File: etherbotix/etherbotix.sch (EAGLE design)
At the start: 28 parts, among them J1 J3011G21DNL, J2 22-03-5035, J3 22-03-5035, J4 22-03-5045, J5 22-03-5045, J6 1760520000, J7 1760490000, J8 502443-0470, J9 502443-0470, U1 STM32F407V, U2 TLK110, U3 OKI-78SR-5/1.5-W36-C, U4 TLV1117-33IKVURG3KVU, U5 ACS711ELCTR-25AB-T, U6 ACS711ELCTR-25AB-T, U7 MAX481CSA, U8 74LS126D, X1 25MHZ

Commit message: routed, still needs cleanup
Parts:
- added ACT: BLUE, fergs:APT1608SGC
- added C1, C2: 2.2uF, fergs:C1608X5R1C225K
- added C10, C14, C15, C16, C23, C24, C25, C26, C3, C36, C37, C38, C5, C6, C7, C8, C9: 0.1uF, fergs:C1608X7R1H104K
- added C11, C27, C28, C31: 4.7uF, fergs:C1608X5R0J475K
- added C12, C19, C20, C21, C22: 1uF, fergs:C1608X5R1H105M
- added C13, C17, C18, C39, C4, C40: 100pF, fergs:C1608C0G1H101J
- added C29, C30, C32: 1000PF, fergs:C1608X7R1H102K
- added C33, C34, C35: 10uF, fergs:C1608X5R0J106M
- added C41: 56uF, fergs:25SVPF56M
- added ERR: RED, fergs:APT1608SGC
- added PWR: GREEN, fergs:APT1608SGC
- added R10, R11, R12, R13, R5, R6, R7, R9: 10k, fergs:P10.0KHCT-ND
- added R14, R15, R16, R17: 49R9, fergs:P49.9HCT-ND
- added R18, R21, R23, R29: 2K2, fergs:P2.20KHCT-ND
- added R19, R20, R24, R25, R26, R28, R8: 1k, fergs:P1.00KHCT-ND
- added R22: 4K87, fergs:P4.87KHCT-ND
- added R27: 15k, fergs:P15.0KHCT-ND
- added R30: 120, fergs:P120HCT-ND
- added R31, R32: 750, fergs:P750HCT-ND
- added X2: (no value), ethernet:ASEMB-50.000MHZ-XY-T
- U3: value OKI-78SR-5/1.5-W36-C -> OKI-78SR-5
- U4: value TLV1117-33IKVURG3KVU -> TLV1117
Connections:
- removed net A3: U$1.P$4, U1.PC3/ETH_MII_TX_CLK/ADC123_IN13(5T)
- removed net ETH_REF_CLK: U1.PA1/ETH_RMII_RX_CLK/ADC123_IN1(5T)
- removed net MCO: U1.PA8/MCO1(5T), U2.XI
- removed net USBDM: U1.PA11/USART1_CTS(5T)
- removed net USBDP: U1.PA12/USART1_RTS(5T)
- new net +12V-AUX: J7.2, MOTORS.VIN, R27.2, U5.IP-1, U5.IP-2
- new net ACT: ACT.A, U1.PC15/OSC32_OUT(5T)
- new net D3: U$1.P$4, U1.PB10/ETH_MII_RX_ER(5T)
- new net ERR: ERR.A, U1.PC14/OSC32_IN(5T)
- new net ETH_CLK: U1.PA1/ETH_RMII_RX_CLK/ADC123_IN1(5T), U2.XI, X2.FO
- new net N$15: C40.1, U1.PH0-OSC_IN(5T), X1G$1.P$2
- new net N$16: J1.TX+, R14.2, U2.TD+
- new net N$17: R18.2, U2.RESERVED
- new net N$18: J1.YELLOW_K, U2.LED_SPEED/AN_1
- new net N$19: J1.RX+, R16.2, U2.RD+
- new net N$20: J1.GREEN_K, U2.LED_ACT/AN_EN
- new net N$21: J1.RX-, R17.1, U2.RD-
- new net N$22: J1.YELLOW_A, R20.1
- new net N$23: J1.GREEN_A, R19.1
- new net N$24: C33.1, C36.1, C37.1, C38.1, U2.PFBIN1, U2.PFBIN2, U2.PFBOUT
- new net N$25: R21.1, U2.SW_STRAP#
- new net N$26: R22.2, U2.RBIAS
- new net N$27: R23.1, U2.RX_DV/MII_MODE
- new net N$28: PWR.C, R26.2
- new net N$30: ERR.C, R25.2
- new net N$31: ACT.C, R24.2
- new net PHY_RST: U1.PE7/TIM1_ETR(5T), U2.RESET#
- new net V_SENSE: R27.1, R28.2, U1.PC0/ADC123_IN10(5T)
- net +12V: now also C41.+; no longer MOTORS.VIN
- net +5V: now also C14.1, C34.1, R10.2, R11.2, R12.2, R13.2, R5.2, R6.2, R7.2
- net A1: now also U1.PC2/ETH_MII_TXD2/ADC123_IN12(5T); no longer U1.PB1/ETH_MII_RXD3/ADC12_IN9(5T)
- net A2: now also U1.PC3/ETH_MII_TX_CLK/ADC123_IN13(5T); no longer U1.PC2/ETH_MII_TXD2/ADC123_IN12(5T)
- net AUX_CURRENT_SENSE: now also U1.PB1/ETH_MII_RXD3/ADC12_IN9(5T)
- net D4: now also U1.PC11/UART4_RX(5T); no longer U1.PB10/ETH_MII_RX_ER(5T)
- net D5: now also U1.PB15/TIM8_CH3N(5T); no longer U1.PC11/UART4_RX(5T)
- net ETH_MDIO: now also R29.1
- net GND: now also C1.2, C10.2, C11.2, C12.2, C13.2, C14.2, C15.2, C16.2, C17.2, C18.2, C19.2, C2.2, C20.2, C21.2, C22.2, C23.2, C24.2, C25.2, C26.2, C27.2, C28.2, C29.2, C3.2, C30.2, C31.2, C32.2, C33.2, C34.2, C35.2, C36.2, C37.2, C38.2, C39.2, C4.2, C40.2, C41.-, C5.2, C6.2, C7.2, C8.2, C9.2, J1.GND, R22.1, R24.1, R25.1, R26.1, R28.1, R32.1, U1.VSSA, X1G$2.G1, X1G$2.G2, X2.GND
- net M1_EN: now also U1.PE13/TIM1_CH3(5T)
- net M1_ENC_A: now also C13.1, U1.PD12/TIM4_CH1(5T); no longer U1.PA6/SPI1_MISO/ADC12_IN6(5T)
- net M1_ENC_B: now also C4.1, U1.PD13/TIM4_CH2(5T)
- net M2_EN: now also U1.PC8/TIM8_CH3(5T)
- net M2_ENC_A: now also C18.1, U1.PA6/SPI1_MISO/ADC12_IN6(5T); no longer U1.PD12/TIM4_CH1(5T)
- net M2_ENC_B: now also C17.1, U1.PB5/TIM3_CH2(5T); no longer U1.PD13/TIM4_CH2(5T)
- net N$1: now also J1.TX-, R15.1, U2.TD-; no longer J7.2, U5.IP-1, U5.IP-2
- net N$10: now also R30.1, R31.1
- net N$11: now also R30.2, R32.2
- net N$12: now also R7.1, R8.1
- net N$13: now also R6.1
- net N$14: now also R8.2
- net N$3: now also C39.1, U1.PH1-OSC_OUT(5T), X1G$1.P$1; no longer U1.VDD_1, U1.VDD_2, U1.VDD_3, U1.VDD_4, U1.VDD_5, U1.VDD_6
- net N$4: now also C1.1
- net N$5: now also C2.1
- net N$6: now also R10.1
- net N$7: now also R11.1
- net N$8: now also R13.1
- net N$9: now also R12.1
- net SERVO_CURRENT_SENSE: now also U1.PA0/ETH_MII_CRS/ADC123_IN0(5T)
- net USART1_RX: now also R9.1
- net USART2_RX: now also R5.1
- net VCC: now also C10.1, C11.1, C12.1, C15.1, C16.1, C19.1, C20.1, C21.1, C22.1, C23.1, C24.1, C25.1, C26.1, C27.1, C28.1, C29.1, C3.1, C30.1, C31.1, C32.1, C35.1, C5.1, C6.1, C7.1, C8.1, C9.1, J1.CT_RX, J1.CT_TX, PWR.A, R14.1, R15.2, R16.1, R17.2, R18.1, R19.2, R20.2, R21.2, R23.2, R29.2, R31.2, R9.2, U1.VDDA, U1.VDD_1, U1.VDD_2, U1.VDD_3, U1.VDD_4, U1.VDD_5, U1.VDD_6, U1.VREF+, U2.AVDD33, U2.VDD_IO, X2.OE, X2.VCC
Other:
- note removed: "0.1uF"
- note removed: "100uF?"
- note removed: "10k"
- note removed: "10k pullup each, 1k inline each, 100pf pull down"
- note removed: "10uF?"
- note removed: "120 between, 750 up/down"
- note removed: "1k"
- note removed: "1uF"
- note removed: "ADD USB"
- note removed: "ENCODER INPUTS"
- moved on the sheet: IMU, J1, J2, J3, J4, J5, J6, J7, J8, J9, JTAG, MOTORS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

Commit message: fix part number of 1760510000
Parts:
- J6: value 1760520000 -> 1760510000; device headers:1760520000 -> headers:1760510000
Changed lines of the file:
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@@
 <part name="J4" library="molex" deviceset="22-03-5045" device=""/>
 <part name="J5" library="molex" deviceset="22-03-5045" device=""/>
-<part name="J6" library="headers" deviceset="1760520000" device=""/>
+<part name="J6" library="headers" deviceset="1760510000" device=""/>
 <part name="J7" library="headers" deviceset="1760490000" device=""/>
 <part name="GND7" library="fergs" deviceset="GND" device=""/>

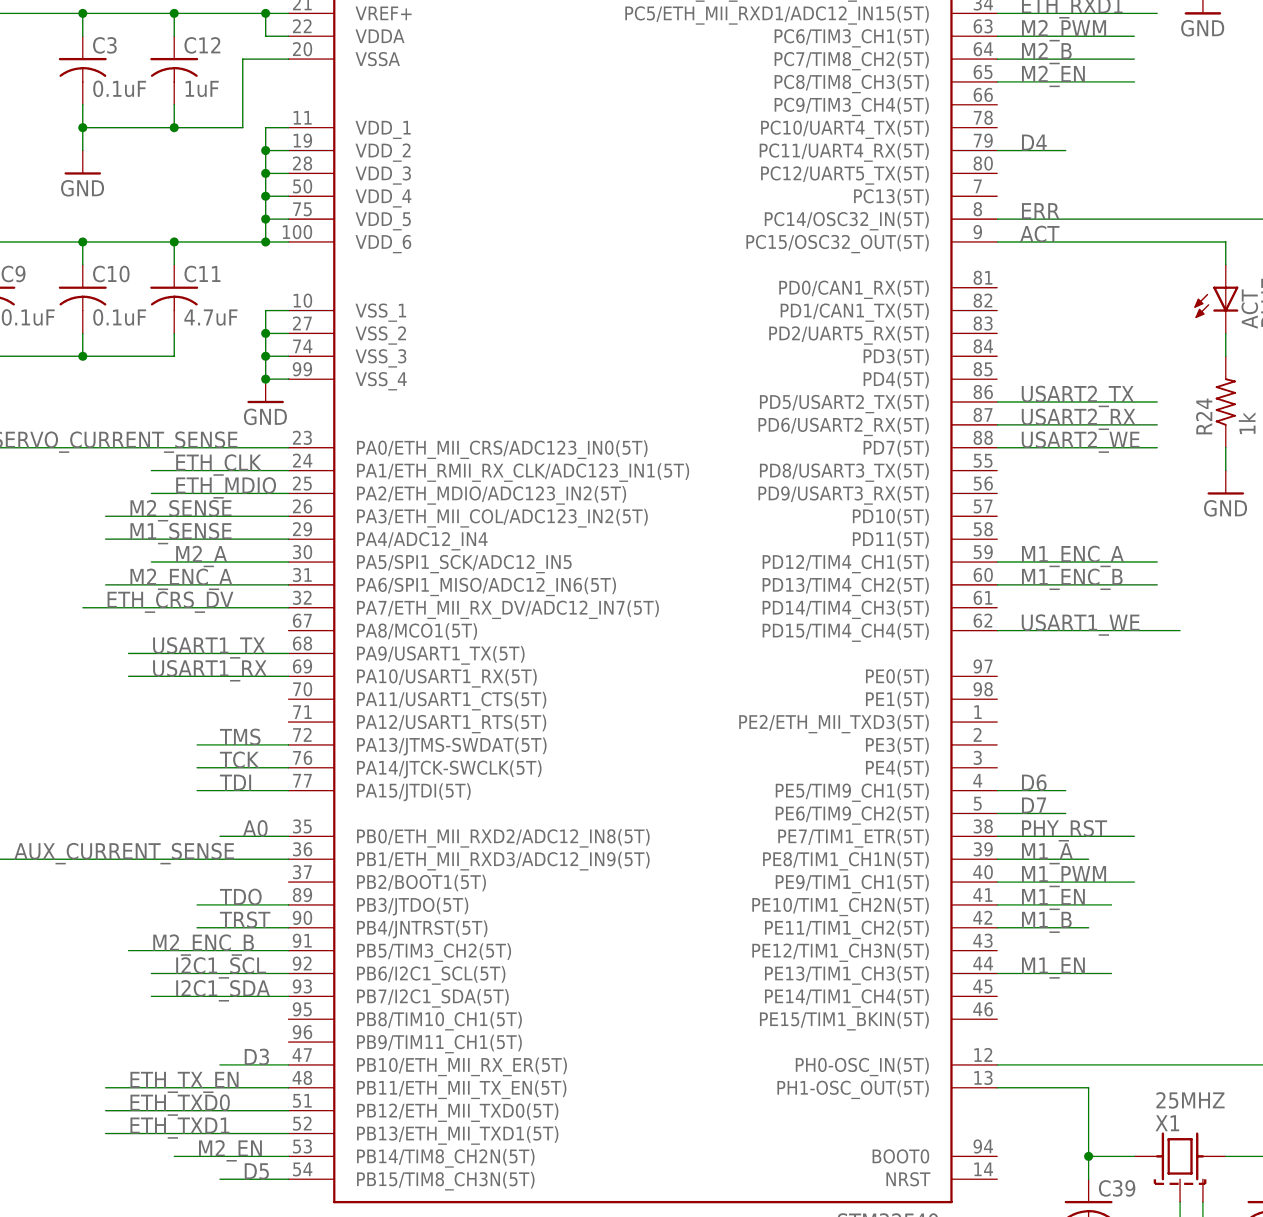
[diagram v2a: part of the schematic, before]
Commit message: add testpads
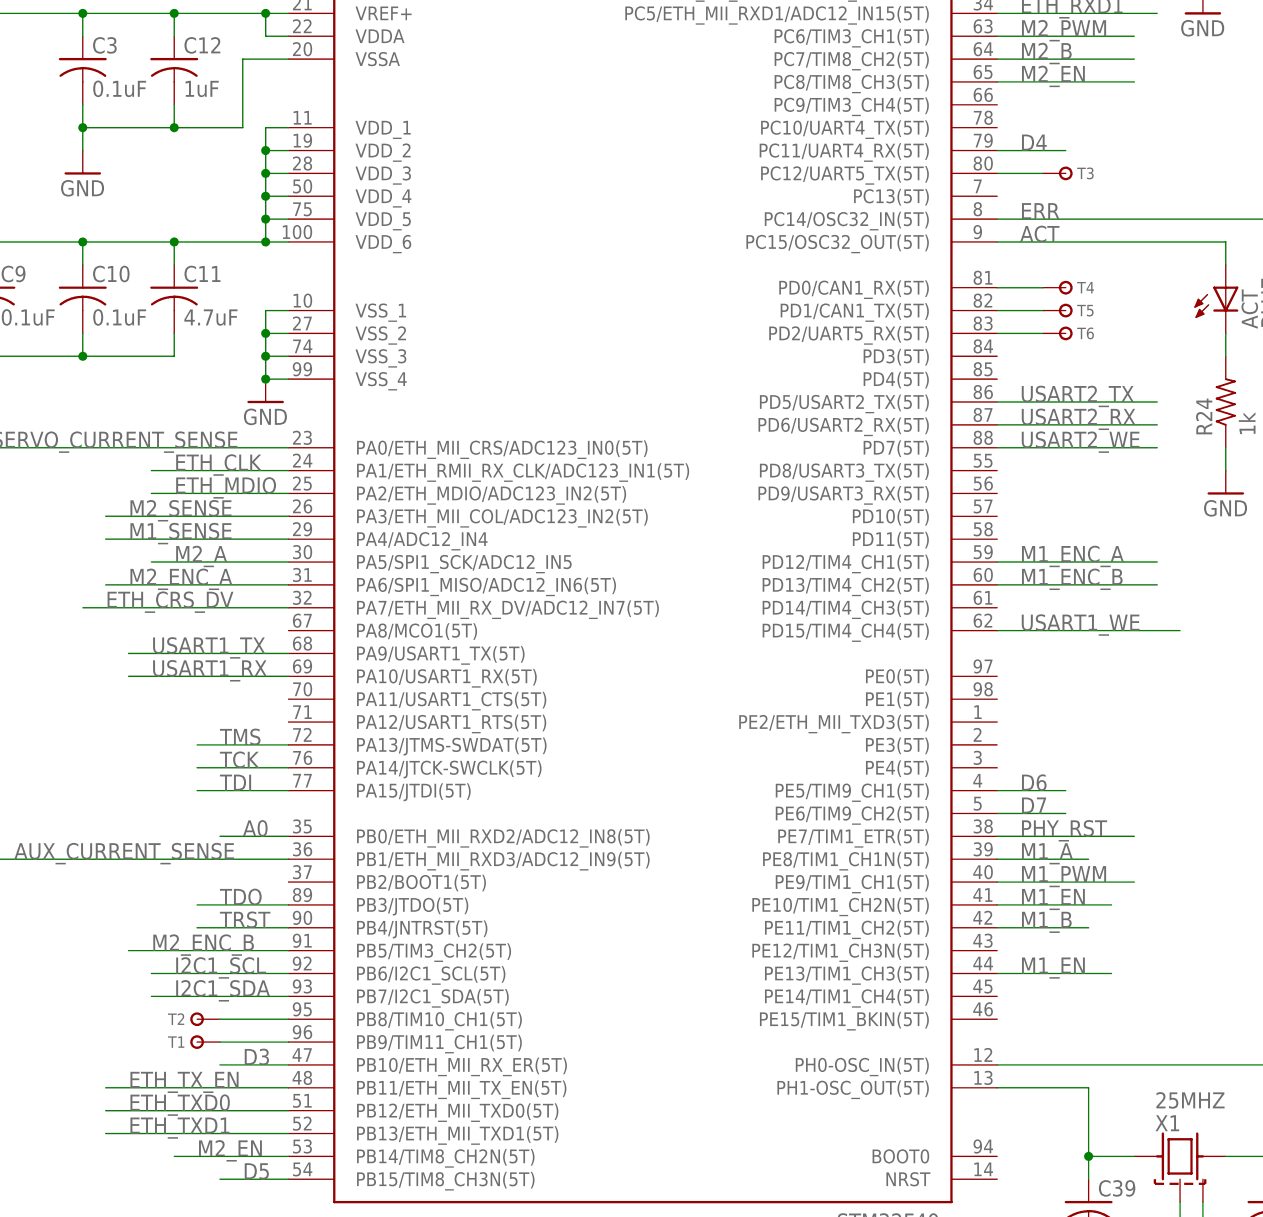
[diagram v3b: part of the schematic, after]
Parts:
- added T1, T2, T3, T4, T5, T6: TESTPAD, fergs:TESTPAD
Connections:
- new net PB8: T2.1, U1.PB8/TIM10_CH1(5T)
- new net PB9: T1.1, U1.PB9/TIM11_CH1(5T)
- new net PC12: T3.1, U1.PC12/UART5_TX(5T)
- new net PD0: T4.1, U1.PD0/CAN1_RX(5T)
- new net PD1: T5.1, U1.PD1/CAN1_TX(5T)
- new net PD2: T6.1, U1.PD2/UART5_RX(5T)
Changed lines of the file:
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@@
 <layers>
 <layer number="1" name="Top" color="4" fill="1" visible="no" active="no"/>
+<layer number="2" name="Route2" color="1" fill="3" visible="no" active="no"/>
+<layer number="3" name="Route3" color="4" fill="3" visible="no" active="no"/>
+<layer number="4" name="Route4" color="1" fill="4" visible="no" active="no"/>
+<layer number="5" name="Route5" color="4" fill="4" visible="no" active="no"/>
+<layer number="6" name="Route6" color="1" fill="8" visible="no" active="no"/>
+<layer number="7" name="Route7" color="4" fill="8" visible="no" active="no"/>
+<layer number="8" name="Route8" color="1" fill="2" visible="no" active="no"/>
+<layer number="9" name="Route9" color="4" fill="2" visible="no" active="no"/>
+<layer number="10" name="Route10" color="1" fill="7" visible="no" active="no"/>
+<layer number="11" name="Route11" color="4" fill="7" visible="no" active="no"/>
+<layer number="12" name="Route12" color="1" fill="5" visible="no" active="no"/>
+<layer number="13" name="Route13" color="4" fill="5" visible="no" active="no"/>
+<layer number="14" name="Route14" color="1" fill="6" visible="no" active="no"/>
+<layer number="15" name="Route15" color="4" fill="6" visible="no" active="no"/>
 <layer number="16" name="Bottom" color="1" fill="1" visible="no" active="no"/>
 <layer number="17" name="Pads" color="2" fill="1" visible="no" active="no"/>
@@
 <part name="R31" library="fergs" deviceset="P750HCT-ND" device="" value="750"/>
 <part name="R32" library="fergs" deviceset="P750HCT-ND" device="" value="750"/>
+<part name="T1" library="fergs" deviceset="TESTPAD" device=""/>
+<part name="T2" library="fergs" deviceset="TESTPAD" device=""/>
+<part name="T3" library="fergs" deviceset="TESTPAD" device=""/>
+<part name="T4" library="fergs" deviceset="TESTPAD" device=""/>
+<part name="T5" library="fergs" deviceset="TESTPAD" device=""/>
+<part name="T6" library="fergs" deviceset="TESTPAD" device=""/>
 </parts>
 <sheets>
@@
 <instance part="R31" gate="G$1" x="429.26" y="99.06" rot="R90"/>
 <instance part="R32" gate="G$1" x="441.96" y="78.74" rot="R90"/>
+<instance part="T1" gate="G$1" x="228.6" y="73.66" rot="R180"/>
+<instance part="T2" gate="G$1" x="228.6" y="76.2" rot="R180"/>
+<instance part="T3" gate="G$1" x="325.12" y="170.18"/>
+<instance part="T4" gate="G$1" x="325.12" y="157.48"/>
+<instance part="T5" gate="G$1" x="325.12" y="154.94"/>
+<instance part="T6" gate="G$1" x="325.12" y="152.4"/>
 </instances>
 <busses>
@@
 </segment>
 </net>
+<net name="PB9" class="0">
+<segment>
+<pinref part="U1" gate="G$1" pin="PB9/TIM11_CH1(5T)"/>
+<pinref part="T1" gate="G$1" pin="1"/>
+<wire x1="238.76" y1="73.66" x2="231.14" y2="73.66" width="0.1524" layer="91"/>
+</segment>
+</net>
+<net name="PB8" class="0">
+<segment>
+<pinref part="U1" gate="G$1" pin="PB8/TIM10_CH1(5T)"/>
+<pinref part="T2" gate="G$1" pin="1"/>
+<wire x1="238.76" y1="76.2" x2="231.14" y2="76.2" width="0.1524" layer="91"/>
+</segment>
+</net>
+<net name="PC12" class="0">
+<segment>
+<pinref part="U1" gate="G$1" pin="PC12/UART5_TX(5T)"/>
+<pinref part="T3" gate="G$1" pin="1"/>
+<wire x1="322.58" y1="170.18" x2="317.5" y2="170.18" width="0.1524" layer="91"/>
+</segment>
+</net>
+<net name="PD0" class="0">
+<segment>
+<pinref part="U1" gate="G$1" pin="PD0/CAN1_RX(5T)"/>
+<pinref part="T4" gate="G$1" pin="1"/>
+<wire x1="322.58" y1="157.48" x2="317.5" y2="157.48" width="0.1524" layer="91"/>
+</segment>
+</net>
+<net name="PD1" class="0">
+<segment>
+<pinref part="U1" gate="G$1" pin="PD1/CAN1_TX(5T)"/>
+<pinref part="T5" gate="G$1" pin="1"/>
+<wire x1="322.58" y1="154.94" x2="317.5" y2="154.94" width="0.1524" layer="91"/>
+</segment>
+</net>
+<net name="PD2" class="0">
+<segment>
+<pinref part="U1" gate="G$1" pin="PD2/UART5_RX(5T)"/>
+<pinref part="T6" gate="G$1" pin="1"/>
+<wire x1="322.58" y1="152.4" x2="317.5" y2="152.4" width="0.1524" layer="91"/>
+</segment>
+</net>
